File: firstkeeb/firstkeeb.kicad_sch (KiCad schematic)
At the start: 2 parts

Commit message: okay so far so good its been 1 hours and the half of the keyboard schematic is done
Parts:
- added D10, D11, D12, D13, D14, D15, D16, D17, D18, D19, D2, D20, D21, D22, D23, D24, D25, D26, D27, D28, D29, D3, D30, D31, D32, D33, D34, D35, D36, D37, D38, D39, D4, D40, D41, D42, D43, D44, D45, D46, D47, D48, D49, D5, D50, D51, D52, D53, D54, D55, D6, D7, D8, D9: 1N4148, Diode_THT:D_DO-35_SOD27_P7.62mm_Horizontal, symbol Diode:1N4148
- added SW1, SW10, SW11, SW12, SW13, SW14, SW15, SW16, SW17, SW18, SW19, SW2, SW20, SW21, SW22, SW23, SW24, SW25, SW26, SW27, SW28, SW29, SW3, SW30, SW31, SW32, SW33, SW34, SW35, SW36, SW37, SW38, SW39, SW4, SW40, SW41, SW42, SW43, SW44, SW45, SW46, SW47, SW48, SW49, SW5, SW50, SW51, SW52, SW53, SW54, SW55, SW6, SW7, SW8, SW9: SW_Push, symbol Switch:SW_Push
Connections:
- net ROW0: now reaches D1.1 (K)
- net ROW0: now also D10.1 (K), D11.1 (K), D12.1 (K), D13.1 (K), D14.1 (K), D15.1 (K), D2.1 (K), D3.1 (K), D4.1 (K), D5.1 (K), D6.1 (K), D7.1 (K), D8.1 (K), D9.1 (K)
- net at D1.2 (A): now also SW1.2
- new net: D18.2 (A), SW18.2
- new net: D39.2 (A), SW39.2
- new net: D14.2 (A), SW14.2
- new net: D3.2 (A), SW3.2
- new net: D43.2 (A), SW43.2
- new net: D29.2 (A), SW29.2
- new net: D17.2 (A), SW17.2
- new net: D54.2 (A), SW54.2
- new net: D16.2 (A), SW16.2
- new net: D34.2 (A), SW34.2
- new net: D9.2 (A), SW9.2
- new net: D19.2 (A), SW19.2
- new net: D5.2 (A), SW5.2
- new net: D36.2 (A), SW36.2
- new net: D49.2 (A), SW49.2
- new net: D32.2 (A), SW32.2
- new net: D48.2 (A), SW48.2
- new net: D52.2 (A), SW52.2
- new net: D38.2 (A), SW38.2
- new net: D25.2 (A), SW25.2
- new net: D4.2 (A), SW4.2
- new net: D21.2 (A), SW21.2
- new net: D28.2 (A), SW28.2
- new net: D8.2 (A), SW8.2
- new net: D53.2 (A), SW53.2
- new net: D7.2 (A), SW7.2
- new net: D41.2 (A), SW41.2
- new net: D12.2 (A), SW12.2
- new net: D46.2 (A), SW46.2
- new net: D6.2 (A), SW6.2
- new net: D47.2 (A), SW47.2
- new net: D30.2 (A), SW30.2
- new net: D44.2 (A), SW44.2
- new net: D2.2 (A), SW2.2
- new net: D31.2 (A), SW31.2
- new net: D15.2 (A), SW15.2
- new net: D40.2 (A), SW40.2
- new net: D35.2 (A), SW35.2
- new net: D33.2 (A), SW33.2
- new net: D27.2 (A), SW27.2
- new net: D55.2 (A), SW55.2
- new net: D20.2 (A), SW20.2
- new net: D13.2 (A), SW13.2
- new net: D42.2 (A), SW42.2
- new net: D50.2 (A), SW50.2
- new net: D23.2 (A), SW23.2
- new net: D51.2 (A), SW51.2
- new net: D45.2 (A), SW45.2
- new net: D24.2 (A), SW24.2
- new net: D26.2 (A), SW26.2
- new net: D22.2 (A), SW22.2
- new net: D11.2 (A), SW11.2
- new net: D37.2 (A), SW37.2
- new net: D10.2 (A), SW10.2
- new net COL0: SW1.1, SW16.1, SW30.1, SW43.1
- new net COL1: SW17.1, SW2.1, SW31.1
- new net COL10: SW11.1, SW26.1, SW40.1, SW52.1
- new net COL11: SW12.1, SW27.1, SW41.1, SW53.1
- new net COL12: SW13.1, SW28.1, SW42.1, SW54.1
- new net COL13: SW14.1, SW29.1, SW55.1
- new net COL14: SW15.1
- new net COL2: SW18.1, SW3.1, SW32.1, SW44.1
- new net COL3: SW19.1, SW33.1, SW4.1, SW45.1
- new net COL4: SW20.1, SW34.1, SW46.1, SW5.1
- new net COL5: SW21.1, SW35.1, SW47.1, SW6.1
- new net COL6: SW22.1, SW36.1, SW48.1, SW7.1
- new net COL7: SW23.1, SW37.1, SW49.1, SW8.1
- new net COL8: SW24.1, SW38.1, SW50.1, SW9.1
- new net COL9: SW10.1, SW25.1, SW39.1, SW51.1
- new net ROW1: D16.1 (K), D17.1 (K), D18.1 (K), D19.1 (K), D20.1 (K), D21.1 (K), D22.1 (K), D23.1 (K), D24.1 (K), D25.1 (K), D26.1 (K), D27.1 (K), D28.1 (K), D29.1 (K)
- new net ROW2: D30.1 (K), D31.1 (K), D32.1 (K), D33.1 (K), D34.1 (K), D35.1 (K), D36.1 (K), D37.1 (K), D38.1 (K), D39.1 (K), D40.1 (K), D41.1 (K), D42.1 (K)
- new net ROW3: D43.1 (K), D44.1 (K), D45.1 (K), D46.1 (K), D47.1 (K), D48.1 (K), D49.1 (K), D50.1 (K), D51.1 (K), D52.1 (K), D53.1 (K), D54.1 (K), D55.1 (K)

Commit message: i finished the keyboard!! (it took a while bc of my laziness and my addiction to the riot games)
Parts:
- added D56, D57, D58, D59, D60, D61, D62, D63, D64, D65, D66, D67, D68, D69, D70, D71, D72, D73, D74, D75, D76, D77, D78, D79: 1N4148, Diode_THT:D_DO-35_SOD27_P7.62mm_Horizontal, symbol Diode:1N4148
- added SW56, SW57, SW58, SW59, SW60, SW61, SW62, SW63, SW64, SW65, SW66, SW67, SW68, SW69, SW70, SW71, SW72, SW73, SW74, SW75, SW76, SW77, SW78, SW79: SW_Push, symbol Switch:SW_Push
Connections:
- net COL0: now also SW56.1, SW68.1
- net COL1: now also SW44.1, SW57.1, SW70.1
- net COL10: now also SW53.1, SW66.1; no longer SW52.1
- net COL11: now also SW54.1, SW67.1; no longer SW53.1
- net COL12: now also SW55.1, SW69.1; no longer SW54.1
- net COL13: now also SW79.1; no longer SW55.1
- net COL14: now also SW78.1
- net COL2: now also SW45.1, SW58.1, SW71.1; no longer SW44.1
- net COL3: now also SW46.1, SW59.1, SW72.1; no longer SW45.1
- net COL4: now also SW47.1, SW60.1, SW73.1; no longer SW46.1
- net COL5: now also SW48.1, SW61.1, SW74.1; no longer SW47.1
- net COL6: now also SW49.1, SW62.1, SW75.1; no longer SW48.1
- net COL7: now also SW50.1, SW63.1, SW76.1; no longer SW49.1
- net COL8: now also SW51.1, SW64.1, SW77.1; no longer SW50.1
- net COL9: now also SW52.1, SW65.1; no longer SW51.1
- new net: D79.2 (A), SW79.2
- new net: D70.2 (A), SW70.2
- new net: D75.2 (A), SW75.2
- new net: D69.2 (A), SW69.2
- new net: D61.2 (A), SW61.2
- new net: D71.2 (A), SW71.2
- new net: D76.2 (A), SW76.2
- new net: D60.2 (A), SW60.2
- new net: D57.2 (A), SW57.2
- new net: D66.2 (A), SW66.2
- new net: D65.2 (A), SW65.2
- new net: D62.2 (A), SW62.2
- new net: D64.2 (A), SW64.2
- new net: D56.2 (A), SW56.2
- new net: D78.2 (A), SW78.2
- new net: D63.2 (A), SW63.2
- new net: D74.2 (A), SW74.2
- new net: D72.2 (A), SW72.2
- new net: D77.2 (A), SW77.2
- new net: D68.2 (A), SW68.2
- new net: D58.2 (A), SW58.2
- new net: D59.2 (A), SW59.2
- new net: D67.2 (A), SW67.2
- new net: D73.2 (A), SW73.2
- new net ROW4: D56.1 (K), D57.1 (K), D58.1 (K), D59.1 (K), D60.1 (K), D61.1 (K), D62.1 (K), D63.1 (K), D64.1 (K), D65.1 (K), D66.1 (K), D67.1 (K), D69.1 (K), D78.1 (K)
- new net ROW5: D68.1 (K), D70.1 (K), D71.1 (K), D72.1 (K), D73.1 (K), D74.1 (K), D75.1 (K), D76.1 (K), D77.1 (K), D79.1 (K)

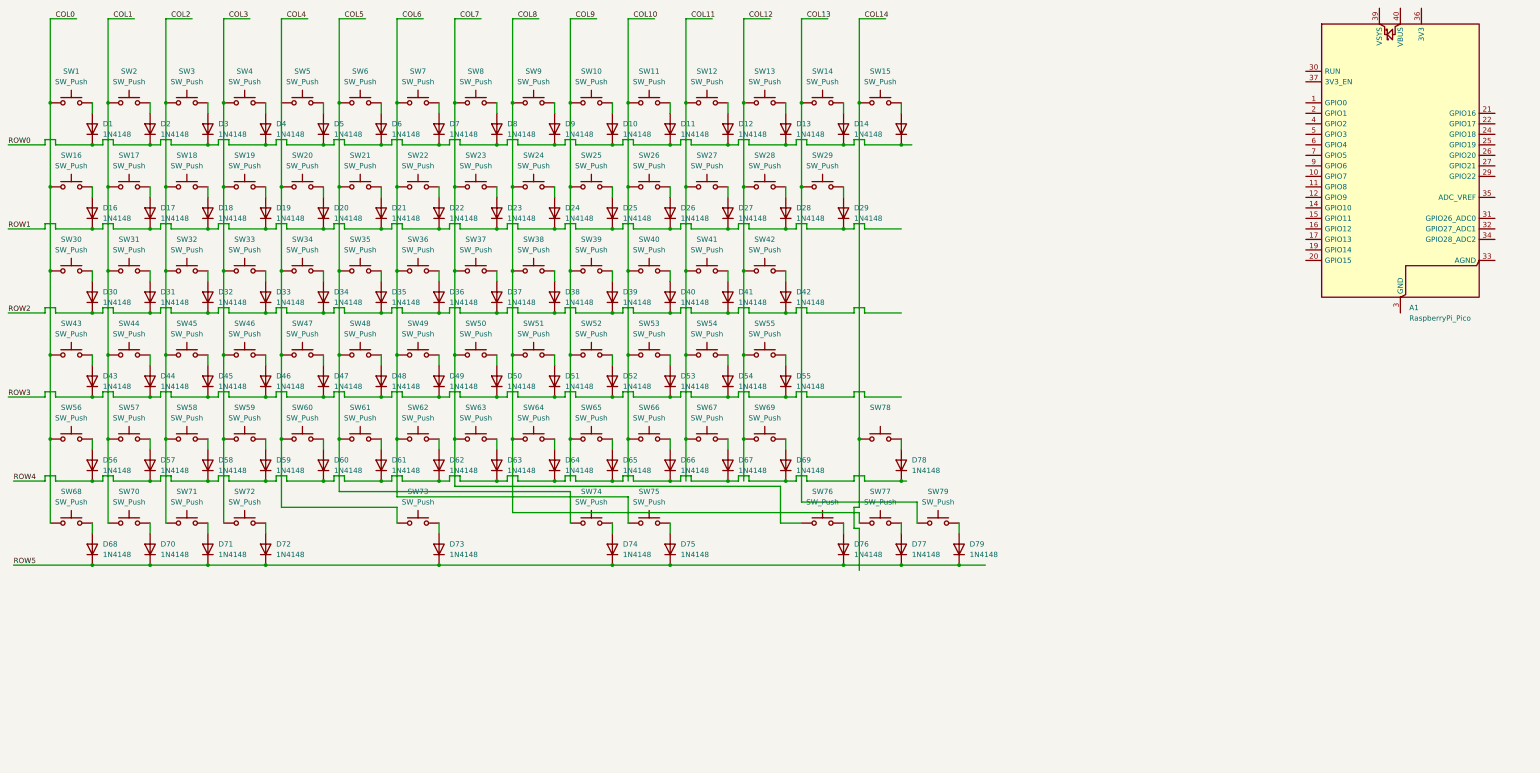
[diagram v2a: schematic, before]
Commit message: i finished the wiring to the microcontroller added the stabilaziers and decided which mount style i will use, i will use top mount
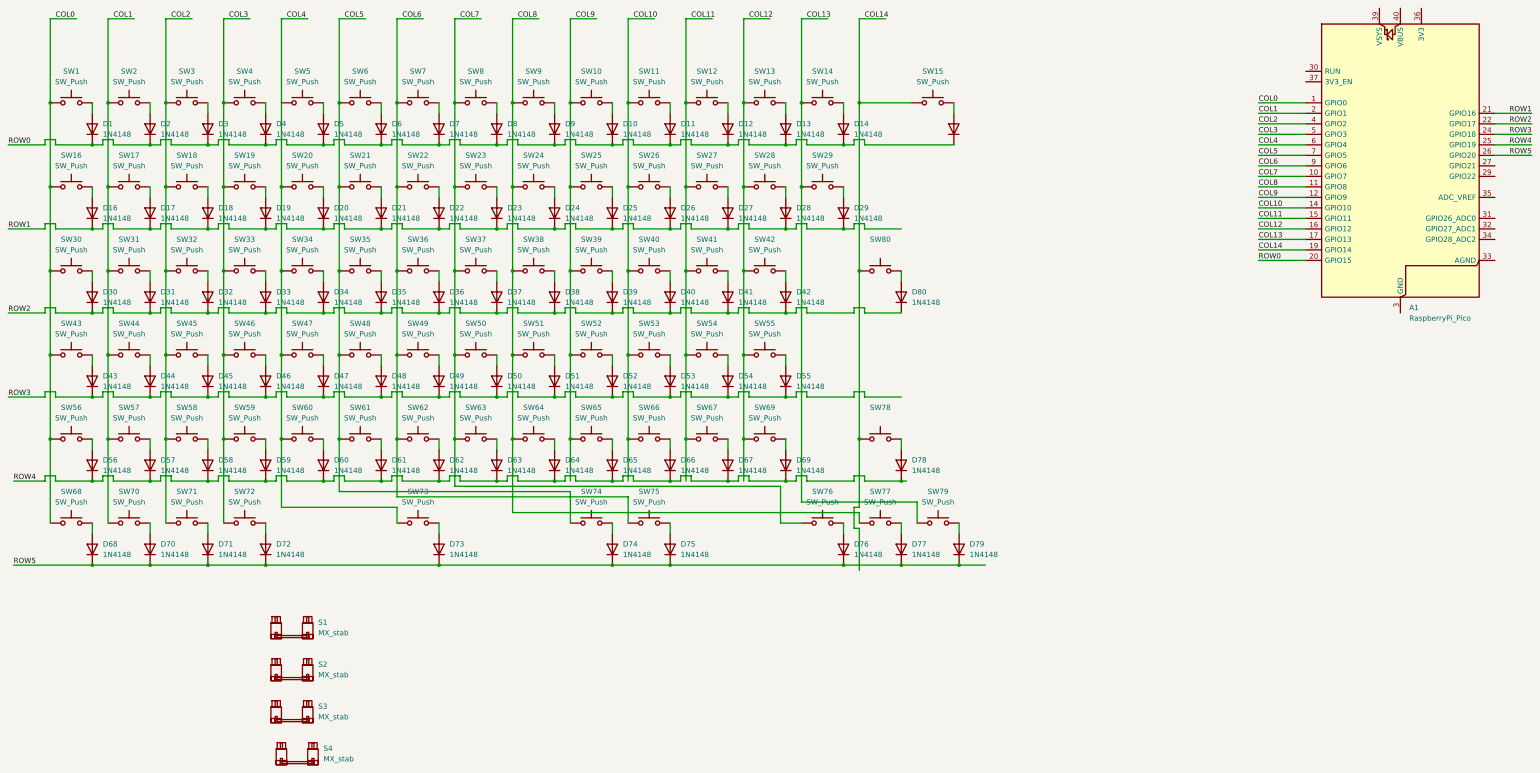
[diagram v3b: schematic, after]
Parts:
- added D80: 1N4148, Diode_THT:D_DO-35_SOD27_P7.62mm_Horizontal, symbol Diode:1N4148
- added S1, S2, S3, S4: MX_stab, PCM_marbastlib-mx:STAB_MX_P_6.25u, symbol PCM_marbastlib-mx:MX_stab
- added SW80: SW_Push, symbol Switch:SW_Push
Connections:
- net COL0: now also A1.1 (GPIO0)
- net COL1: now also A1.2 (GPIO1)
- net COL10: now also A1.14 (GPIO10)
- net COL11: now also A1.15 (GPIO11)
- net COL12: now also A1.16 (GPIO12)
- net COL13: now also A1.17 (GPIO13)
- net COL14: now also A1.19 (GPIO14), SW80.1
- net COL2: now also A1.4 (GPIO2)
- net COL3: now also A1.5 (GPIO3)
- net COL4: now also A1.6 (GPIO4)
- net COL5: now also A1.7 (GPIO5)
- net COL6: now also A1.9 (GPIO6)
- net COL7: now also A1.10 (GPIO7)
- net COL8: now also A1.11 (GPIO8)
- net COL9: now also A1.12 (GPIO9)
- net ROW0: now also A1.20 (GPIO15)
- net ROW1: now also A1.21 (GPIO16)
- net ROW2: now also A1.22 (GPIO17), D80.1 (K)
- net ROW3: now also A1.24 (GPIO18)
- net ROW4: now also A1.25 (GPIO19)
- net ROW5: now also A1.26 (GPIO20)
- new net: D80.2 (A), SW80.2
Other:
- moved on the sheet: SW15
